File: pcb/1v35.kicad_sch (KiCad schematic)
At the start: 5 parts, among them U12 TPSM82903

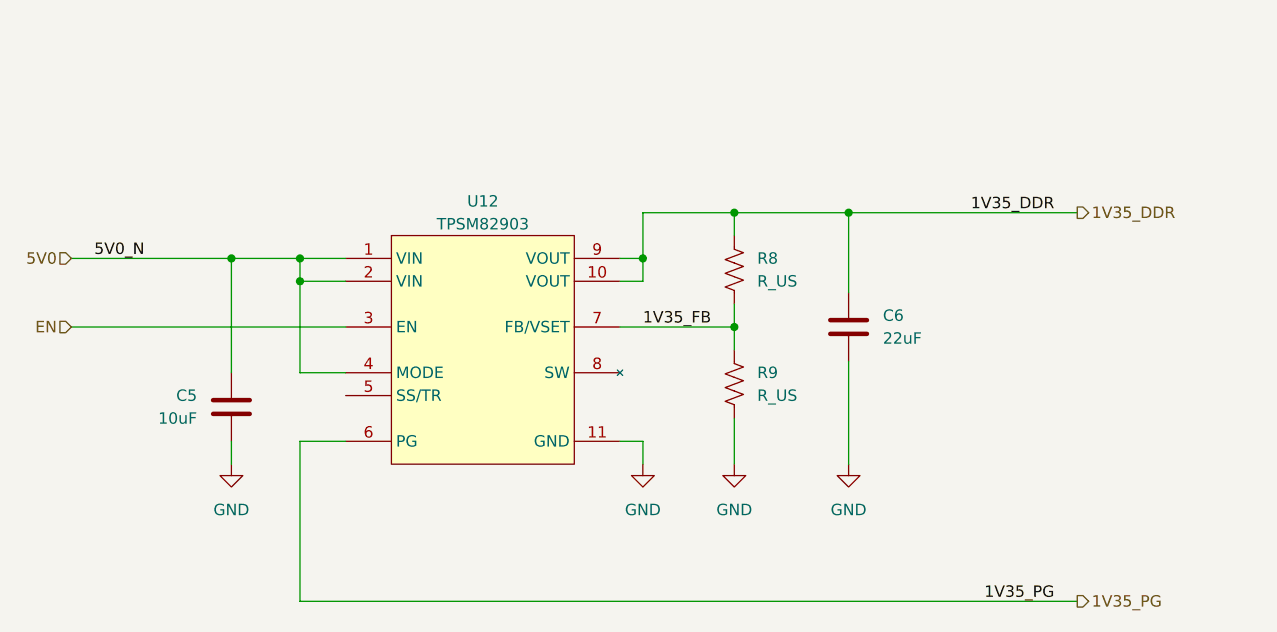
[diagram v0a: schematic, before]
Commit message: changes to power tree
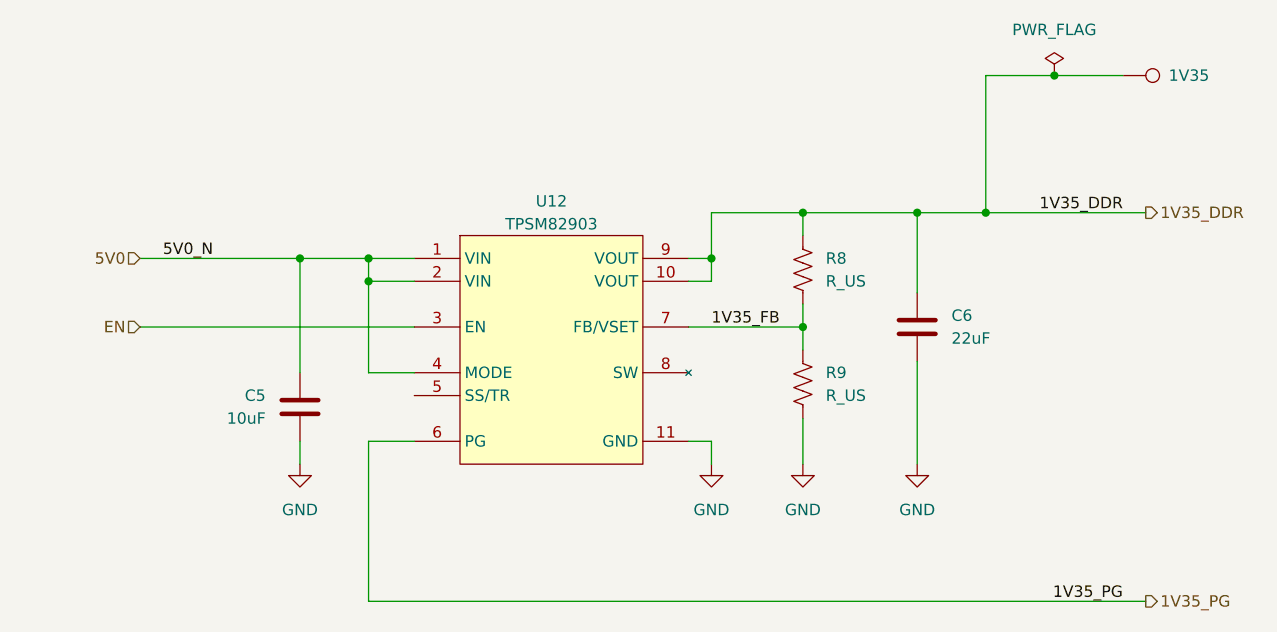
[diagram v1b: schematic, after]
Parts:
- added 1V35: TestPoint, TestPoint:TestPoint_Pad_D1.0mm, symbol library:TestPoint
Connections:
- net 1V35_DDR: now also 1V35.1
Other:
- moved on the sheet: C5, C6, R8, R9, U12

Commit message: moved stuff around, bom
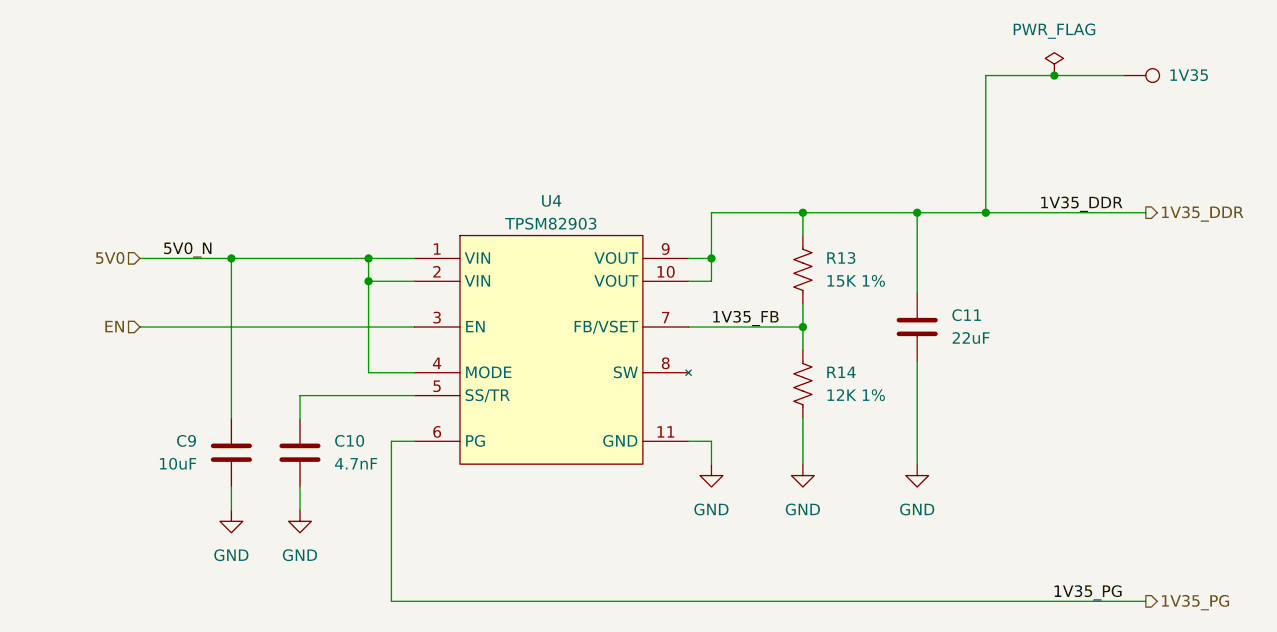
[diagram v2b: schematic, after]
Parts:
- removed C5: 10uF, symbol library:C
- added C10: 4.7nF, Capacitor_SMD:C_0402_1005Metric, symbol library:C
- added C9: 10uF, symbol library:C
- R13: renamed from R8; value R_US -> 15K 1%
- R14: renamed from R9; value R_US -> 12K 1%
- renumbered C6 to C11, U12 to U4
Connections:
- net 5V0: now also C9.1
- net GND: now also C10.2, C9.2
- net at U4.5 (SS/TR): now also C10.1

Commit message: bom
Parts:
- 1V35: now left out of the parts list
- C10: Part Description (none) -> CAP CER 0402 4.7NF 50V X7R 5%
- C11: footprint (none) -> Capacitor_SMD:C_0603_1608Metric; Manufacturer (none) -> Murata Electronics; Manufacturer Product Number (none) -> GRM188R61A226ME15D; Part Description (none) -> CAP CER 22UF 10V X5R 0603
- C9: footprint (none) -> Capacitor_SMD:C_0402_1005Metric; Manufacturer (none) -> Murata Electronics; Manufacturer Product Number (none) -> GRM155R61A106ME11D; Part Description (none) -> CAP CER 10UF 10V X5R 0402
- R14: renamed from R13; footprint (none) -> Resistor_SMD:R_0402_1005Metric; Manufacturer (none) -> Vishay Dale; Manufacturer Product Number (none) -> CRCW040215K0FKED; Part Description (none) -> RES 15K OHM 1% 1/16W 0402
- R15: renamed from R14; footprint (none) -> Resistor_SMD:R_0402_1005Metric; Manufacturer (none) -> Vishay Dale; Manufacturer Product Number (none) -> CRCW040212K0FKED; Part Description (none) -> RES 12K OHM 1% 1/16W 0402
- U4: Part Description (none) -> 3-V TO 17-V, 3-A, HIGH-EFFICIENC
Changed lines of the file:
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@@
 		(dnp no)
 		(fields_autoplaced yes)
-		(property "Reference" "R13"
+		(property "Reference" "R14"
 			(at 165.1 83.8199 0)
 			(effects
@@
 			)
 		)
-		(property "Footprint" ""
+		(property "Footprint" "Resistor_SMD:R_0402_1005Metric"
 			(at 163.576 85.344 90)
 			(effects
@@
 			)
 		)
+		(property "Manufacturer" "Vishay Dale"
+			(at 162.56 85.09 0)
+			(effects
+				(font
+					(size 1.27 1.27)
+				)
+				(hide yes)
+			)
+		)
+		(property "Manufacturer Product Number" "CRCW040215K0FKED"
+			(at 162.56 85.09 0)
+			(effects
+				(font
+					(size 1.27 1.27)
+				)
+				(hide yes)
+			)
+		)
+		(property "Part Description" "RES 15K OHM 1% 1/16W 0402"
+			(at 162.56 85.09 0)
+			(effects
+				(font
+					(size 1.27 1.27)
+				)
+				(hide yes)
+			)
+		)
 		(pin "1"
 		)
@@
 			(project "RPi-HwAB-1"
 				(path "/e63e39d7-6ac0-4ffd-8aa3-1841a4541b55/f9ebb56c-78c7-42ac-bc19-ccbf788f5318/ac4b7fa8-6267-4e3b-81b7-39bc9eb5247a"
-					(reference "R13")
+					(reference "R14")
 					(unit 1)
 				)
@@
 			)
 		)
+		(property "Part Description" "3-V TO 17-V, 3-A, HIGH-EFFICIENC"
+			(at 134.62 93.98 0)
+			(effects
+				(font
+					(size 1.27 1.27)
+				)
+				(hide yes)
+			)
+		)
 		(pin "11"
 		)
@@
 		(dnp no)
 		(fields_autoplaced yes)
-		(property "Reference" "R14"
+		(property "Reference" "R15"
 			(at 165.1 96.5199 0)
 			(effects
@@
 			)
 		)
-		(property "Footprint" ""
+		(property "Footprint" "Resistor_SMD:R_0402_1005Metric"
 			(at 163.576 98.044 90)
 			(effects
@@
 			)
 		)
+		(property "Manufacturer" "Vishay Dale"
+			(at 162.56 97.79 0)
+			(effects
+				(font
+					(size 1.27 1.27)
+				)
+				(hide yes)
+			)
+		)
+		(property "Manufacturer Product Number" "CRCW040212K0FKED"
+			(at 162.56 97.79 0)
+			(effects
+				(font
+					(size 1.27 1.27)
+				)
+				(hide yes)
+			)
+		)
+		(property "Part Description" "RES 12K OHM 1% 1/16W 0402"
+			(at 162.56 97.79 0)
+			(effects
+				(font
+					(size 1.27 1.27)
+				)
+				(hide yes)
+			)
+		)
 		(pin "1"
 		)
@@
 			(project "RPi-HwAB-1"
 				(path "/e63e39d7-6ac0-4ffd-8aa3-1841a4541b55/f9ebb56c-78c7-42ac-bc19-ccbf788f5318/ac4b7fa8-6267-4e3b-81b7-39bc9eb5247a"
-					(reference "R14")
+					(reference "R15")
 					(unit 1)
 				)
@@
 			)
 		)
-		(property "Datasheet" ""
+		(property "Datasheet" "~"
 			(at 106.68 105.41 0)
 			(effects
@@
 		)
 		(property "Manufacturer Product Number" "C0402C472J5RECTU"
+			(at 106.68 105.41 0)
+			(effects
+				(font
+					(size 1.27 1.27)
+				)
+				(hide yes)
+			)
+		)
+		(property "Part Description" "CAP CER 0402 4.7NF 50V X7R 5%"
 			(at 106.68 105.41 0)
 			(effects
@@
 		(unit 1)
 		(exclude_from_sim no)
-		(in_bom yes)
+		(in_bom no)
 		(on_board yes)
 		(dnp no)
@@
 			)
 		)
+		(property "Name" ""
+			(at 198.12 63.5 0)
+			(effects
+				(font
+					(size 1.27 1.27)
+				)
+				(hide yes)
+			)
+		)
 		(pin "1"
 		)
@@
 			)
 		)
-		(property "Footprint" ""
+		(property "Footprint" "Capacitor_SMD:C_0402_1005Metric"
 			(at 100.0252 109.22 0)
 			(effects
@@
 		)
 		(property "Description" "Unpolarized capacitor"
+			(at 99.06 105.41 0)
+			(effects
+				(font
+					(size 1.27 1.27)
+				)
+				(hide yes)
+			)
+		)
+		(property "Manufacturer" "Murata Electronics"
+			(at 99.06 105.41 0)
+			(effects
+				(font
+					(size 1.27 1.27)
+				)
+				(hide yes)
+			)
+		)
+		(property "Manufacturer Product Number" "GRM155R61A106ME11D"
+			(at 99.06 105.41 0)
+			(effects
+				(font
+					(size 1.27 1.27)
+				)
+				(hide yes)
+			)
+		)
+		(property "Part Description" "CAP CER 10UF 10V X5R 0402"
 			(at 99.06 105.41 0)
 			(effects
@@
 			)
 		)
-		(property "Footprint" ""
+		(property "Footprint" "Capacitor_SMD:C_0603_1608Metric"
 			(at 174.2948 95.25 0)
 			(effects
@@
 			(at 175.26 91.44 0)
 			(effects
+				(font
+					(size 1.27 1.27)
+				)
+				(hide yes)
+			)
+		)
+		(property "Manufacturer" "Murata Electronics"
+			(at 175.26 91.44 0)
+			(effects
+				(font
+					(size 1.27 1.27)
+				)
+				(hide yes)
+			)
+		)
+		(property "Manufacturer Product Number" "GRM188R61A226ME15D"
+			(at 175.26 91.44 0)
+			(effects
+				(font
+					(size 1.27 1.27)
+				)
+				(hide yes)
+			)
+		)
+		(property "Part Description" "CAP CER 22UF 10V X5R 0603"
+			(at 175.26 91.44 0)
+			(effects

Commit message: added mig ddr pinout constraints
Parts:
- C10: renamed from C9; footprint Capacitor_SMD:C_0402_1005Metric -> Capacitor_SMD:C_1206_3216Metric; Manufacturer Murata Electronics -> KYOCERA AVX; Manufacturer Product Number GRM155R61A106ME11D -> TAJA106M010RNJ; Part Description CAP CER 10UF 10V X5R 0402 -> CAP TANT 10UF 20% 10V 1206
- renumbered C10 to C11, C11 to C9
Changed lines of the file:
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@@
 		(dnp no)
 		(fields_autoplaced yes)
-		(property "Reference" "#PWR015"
+		(property "Reference" "#PWR013"
 			(at 162.56 113.03 0)
 			(effects
@@
 			(project "RPi-HwAB-1"
 				(path "/e63e39d7-6ac0-4ffd-8aa3-1841a4541b55/f9ebb56c-78c7-42ac-bc19-ccbf788f5318/ac4b7fa8-6267-4e3b-81b7-39bc9eb5247a"
-					(reference "#PWR015")
+					(reference "#PWR013")
 					(unit 1)
 				)
@@
 		(on_board yes)
 		(dnp no)
-		(property "Reference" "C10"
+		(property "Reference" "C11"
 			(at 110.49 104.14 0)
 			(effects
@@
 			(project "RPi-HwAB-1"
 				(path "/e63e39d7-6ac0-4ffd-8aa3-1841a4541b55/f9ebb56c-78c7-42ac-bc19-ccbf788f5318/ac4b7fa8-6267-4e3b-81b7-39bc9eb5247a"
-					(reference "C10")
+					(reference "C11")
 					(unit 1)
 				)
@@
 		(dnp no)
 		(fields_autoplaced yes)
-		(property "Reference" "#PWR014"
+		(property "Reference" "#PWR012"
 			(at 152.4 113.03 0)
 			(effects
@@
 			(project "RPi-HwAB-1"
 				(path "/e63e39d7-6ac0-4ffd-8aa3-1841a4541b55/f9ebb56c-78c7-42ac-bc19-ccbf788f5318/ac4b7fa8-6267-4e3b-81b7-39bc9eb5247a"
-					(reference "#PWR014")
+					(reference "#PWR012")
 					(unit 1)
 				)
@@
 		(on_board yes)
 		(dnp no)
-		(property "Reference" "C9"
+		(property "Reference" "C10"
 			(at 95.25 104.1399 0)
 			(effects
@@
 			)
 		)
-		(property "Footprint" "Capacitor_SMD:C_0402_1005Metric"
+		(property "Footprint" "Capacitor_SMD:C_1206_3216Metric"
 			(at 100.0252 109.22 0)
 			(effects
@@
 			)
 		)
-		(property "Manufacturer" "Murata Electronics"
+		(property "Manufacturer" "KYOCERA AVX"
 			(at 99.06 105.41 0)
 			(effects
@@
 			)
 		)
-		(property "Manufacturer Product Number" "GRM155R61A106ME11D"
+		(property "Manufacturer Product Number" "TAJA106M010RNJ"
 			(at 99.06 105.41 0)
 			(effects
@@
 			)
 		)
-		(property "Part Description" "CAP CER 10UF 10V X5R 0402"
+		(property "Part Description" "CAP TANT 10UF 20% 10V 1206"
 			(at 99.06 105.41 0)
 			(effects
@@
 			(project "RPi-HwAB-1"
 				(path "/e63e39d7-6ac0-4ffd-8aa3-1841a4541b55/f9ebb56c-78c7-42ac-bc19-ccbf788f5318/ac4b7fa8-6267-4e3b-81b7-39bc9eb5247a"
-					(reference "C9")
+					(reference "C10")
 					(unit 1)
 				)
@@
 		(dnp no)
 		(fields_autoplaced yes)
-		(property "Reference" "#PWR013"
+		(property "Reference" "#PWR016"
 			(at 106.68 118.11 0)
 			(effects
@@
 			(project "RPi-HwAB-1"
 				(path "/e63e39d7-6ac0-4ffd-8aa3-1841a4541b55/f9ebb56c-78c7-42ac-bc19-ccbf788f5318/ac4b7fa8-6267-4e3b-81b7-39bc9eb5247a"
-					(reference "#PWR013")
+					(reference "#PWR016")
 					(unit 1)
 				)
@@
 		(dnp no)
 		(fields_autoplaced yes)
-		(property "Reference" "#PWR012"
+		(property "Reference" "#PWR015"
 			(at 99.06 118.11 0)
 			(effects
@@
 			(project "RPi-HwAB-1"
 				(path "/e63e39d7-6ac0-4ffd-8aa3-1841a4541b55/f9ebb56c-78c7-42ac-bc19-ccbf788f5318/ac4b7fa8-6267-4e3b-81b7-39bc9eb5247a"
-					(reference "#PWR012")
+					(reference "#PWR015")
 					(unit 1)
 				)
@@
 		(dnp no)
 		(fields_autoplaced yes)
-		(property "Reference" "#PWR016"
+		(property "Reference" "#PWR014"
 			(at 175.26 113.03 0)
 			(effects
@@
 			(project "RPi-HwAB-1"
 				(path "/e63e39d7-6ac0-4ffd-8aa3-1841a4541b55/f9ebb56c-78c7-42ac-bc19-ccbf788f5318/ac4b7fa8-6267-4e3b-81b7-39bc9eb5247a"
-					(reference "#PWR016")
+					(reference "#PWR014")
 					(unit 1)
 				)
@@
 		(on_board yes)
 		(dnp no)
-		(property "Reference" "C11"
+		(property "Reference" "C9"
 			(at 179.07 90.1699 0)
 			(effects
@@
 			(project "RPi-HwAB-1"
 				(path "/e63e39d7-6ac0-4ffd-8aa3-1841a4541b55/f9ebb56c-78c7-42ac-bc19-ccbf788f5318/ac4b7fa8-6267-4e3b-81b7-39bc9eb5247a"
-					(reference "C11")
-					(unit 1)
-				)
+					(reference "C9")
+					(unit 1)
+				)
